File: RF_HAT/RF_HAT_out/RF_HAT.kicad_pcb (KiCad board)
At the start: 8 copper layers, 56 x 65 mm, 97 parts, among them J1 SMA, J2 SMA, J3 Raspberry_Pi_2_3, U1 CC1200RHBR, U2 CC1200RHBR, U3 RaspberryPi_Pico, U4 XT30PW-M, U5 LMR51420YFDDCR, Y1 40MHz, Y2 40MHz

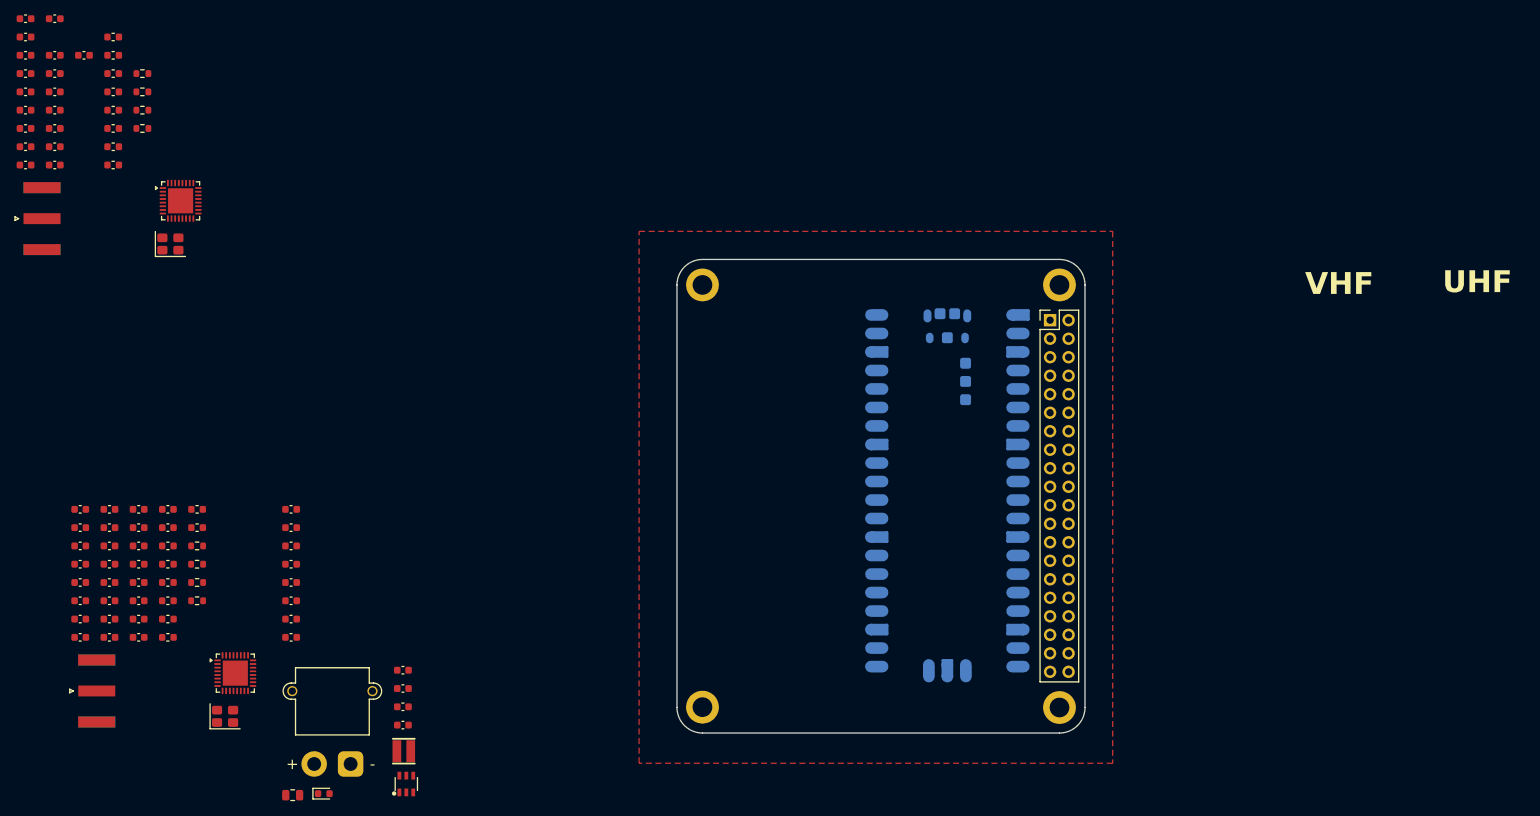
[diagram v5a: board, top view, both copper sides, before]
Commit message: did final routing and added Farnell and LCSC numbers to all components
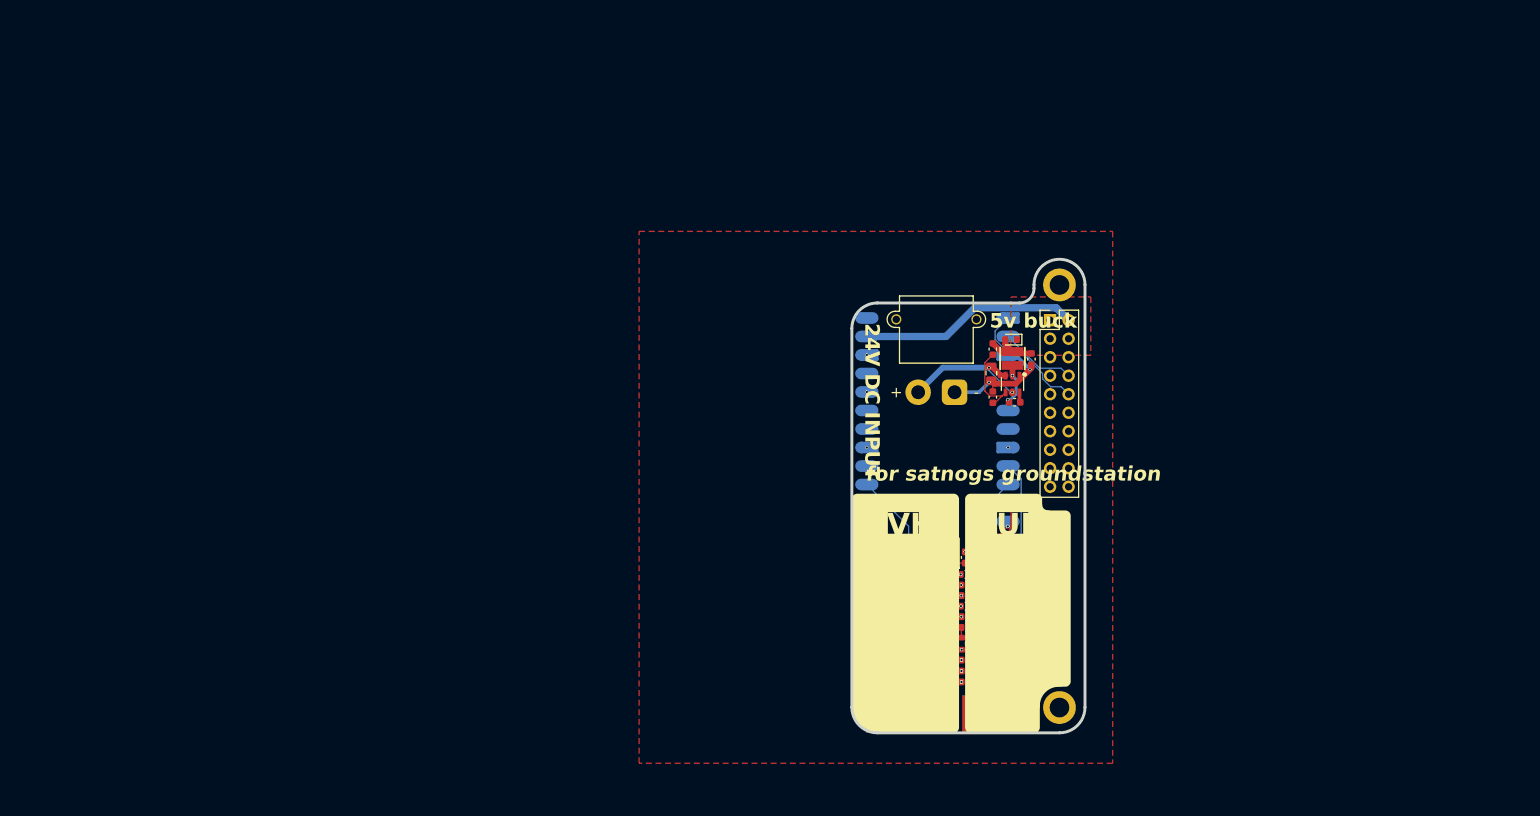
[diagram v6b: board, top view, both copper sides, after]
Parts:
- removed H2, H3: MountingHole_Pad, MountingHole:MountingHole_2.7mm_M2.5_ISO7380_Pad
- moved C1 160.1 mm to (205.9, 116.8), turned to -90 degrees
- moved C10 159.8 mm to (204.2, 124.2), turned to -90 degrees
- moved C3 158.7 mm to (207.4, 116.8), turned to 90 degrees
- moved C12 155.8 mm to (214.9, 105.0), turned to -90 degrees
- moved C2 155.0 mm to (204.2, 112.4), turned to -90 degrees
- moved C4 153.9 mm to (202.0, 118.8), turned to 180 degrees
- moved C8 153.7 mm to (210.4, 113.9), turned to -90 degrees
- moved C14 153.2 mm to (212.6, 108.7)
- moved C5 150.4 mm to (202.8, 113.6), turned to 90 degrees
- moved C13 150.3 mm to (213.1, 98.6)
- moved C15 150.1 mm to (212.6, 104.3)
- moved C21 150.0 mm to (208.9, 110.9), turned to -90 degrees
- moved C9 149.9 mm to (207.4, 113.9), turned to -90 degrees
- moved C6 149.7 mm to (202.0, 115.8), turned to 180 degrees
- moved C7 149.2 mm to (202.0, 117.3), turned to 180 degrees
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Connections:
- J3 pad 10: /Pi_Header/UART_RX -> /Pi_Header/UART_TX
- J3 pad 8: /Pi_Header/UART_TX -> /Pi_Header/UART_RX
- R1 pad 2: /CC1200_VHF_144MHz/UHF_CSN -> /CC1200_VHF_144MHz/VHF_CSN
- R2 pad 2: /CC1200_VHF_144MHz/UHF_RESET -> /CC1200_VHF_144MHz/VHF_RESET
- U2 pad 10: /CC1200_VHF_144MHz/UHF_GPIO0 -> /CC1200_VHF_144MHz/VHF_GPIO0
- U2 pad 11: /CC1200_VHF_144MHz/UHF_CSN -> /CC1200_VHF_144MHz/VHF_CSN
- U2 pad 2: /CC1200_VHF_144MHz/UHF_RESET -> /CC1200_VHF_144MHz/VHF_RESET
- U2 pad 3: /CC1200_VHF_144MHz/UHF_GPIO3 -> /CC1200_VHF_144MHz/VHF_GPIO3
- U2 pad 4: /CC1200_VHF_144MHz/UHF_GPIO2 -> /CC1200_VHF_144MHz/VHF_GPIO2
- U2 pad 7: /CC1200_VHF_144MHz/UHF_MOSI -> /CC1200_VHF_144MHz/VHF_MOSI
- U2 pad 8: /CC1200_VHF_144MHz/UHF_SCLK -> /CC1200_VHF_144MHz/VHF_SCLK
- U2 pad 9: /CC1200_VHF_144MHz/UHF_MISO -> /CC1200_VHF_144MHz/VHF_MISO
- U3 pad 21: /Pico_SPI_Host/VHF_MISO -> /CC1200_VHF_144MHz/VHF_MISO
- U3 pad 22: /Pico_SPI_Host/VHF_CSN -> /CC1200_VHF_144MHz/VHF_CSN
- U3 pad 24: /Pico_SPI_Host/VHF_SCLK -> /CC1200_VHF_144MHz/VHF_SCLK
- U3 pad 25: /Pico_SPI_Host/VHF_MOSI -> /CC1200_VHF_144MHz/VHF_MOSI
- U3 pad 26: /Pico_SPI_Host/VHF_RESET -> /CC1200_VHF_144MHz/VHF_RESET
- U3 pad 27: /Pico_SPI_Host/VHF_GPIO2 -> /CC1200_VHF_144MHz/VHF_GPIO2
- U3 pad 29: /Pico_SPI_Host/VHF_GPIO0 -> /CC1200_VHF_144MHz/VHF_GPIO0
- U3 pad 31: /Pico_SPI_Host/VHF_GPIO3 -> /CC1200_VHF_144MHz/VHF_GPIO3
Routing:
- net +3V3: track 0.00 -> 56.9 mm, vias 0 -> 31
- net GND: track 0.00 -> 34.7 mm, vias 0 -> 59
- net +5V: track 0.00 -> 30.0 mm
- net +24V: track 0.00 -> 18.9 mm, vias 0 -> 2
- net /Pi_Header/UART_TX: track 0.00 -> 17.3 mm
- net /CC1200_UHF_432MHz/UHF_GPIO3: track 0.00 -> 16.7 mm, vias 0 -> 1
- net /CC1200_VHF_144MHz/VHF_MISO: track 0.00 -> 15.6 mm, vias 0 -> 1
- net /CC1200_UHF_432MHz/UHF_GPIO0: track 0.00 -> 15.3 mm, vias 0 -> 1
- net /CC1200_VHF_144MHz/VHF_GPIO3: track 0.00 -> 14.1 mm, vias 0 -> 1
- net /CC1200_VHF_144MHz/VHF_CSN: track 0.00 -> 13.7 mm, vias 0 -> 1
- net Net-(U1-TRX_SW): track 0.00 -> 11.5 mm
- net Net-(U2-TRX_SW): track 0.00 -> 11.2 mm
- net /Pi_Header/UART_RX: track 0.00 -> 10.5 mm
- net Net-(U5-FB): track 0.00 -> 10.4 mm
- net /CC1200_UHF_432MHz/UHF_RESET: track 0.00 -> 10.3 mm, vias 0 -> 1
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- added copper zone on In2.Cu, net +3V3
- added copper zone on In3.Cu, net +3V3
- added copper zone on F.Cu, net GND
- added copper zone on In4.Cu, net GND
- removed copper zone on In4.Cu, net (none)
- removed copper zone on In4.Cu, net +3V3
- removed copper zone on In3.Cu, net GND
- removed copper zone on In5.Cu, net GND
- removed copper zone on In6.Cu, net GND
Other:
- board size 56 x 65 mm -> 32 x 65 mm
- copper layers 8 -> 6
- board text added: "-RF HAT-"
- board text added: "24V DC INPUT"
- board text added: "5v buck"
- board text added: "connect to any pi ----"
- board text added: "for satnogs groundstation"
- board text added: "pi zero, pi3, pi4, pi5..."

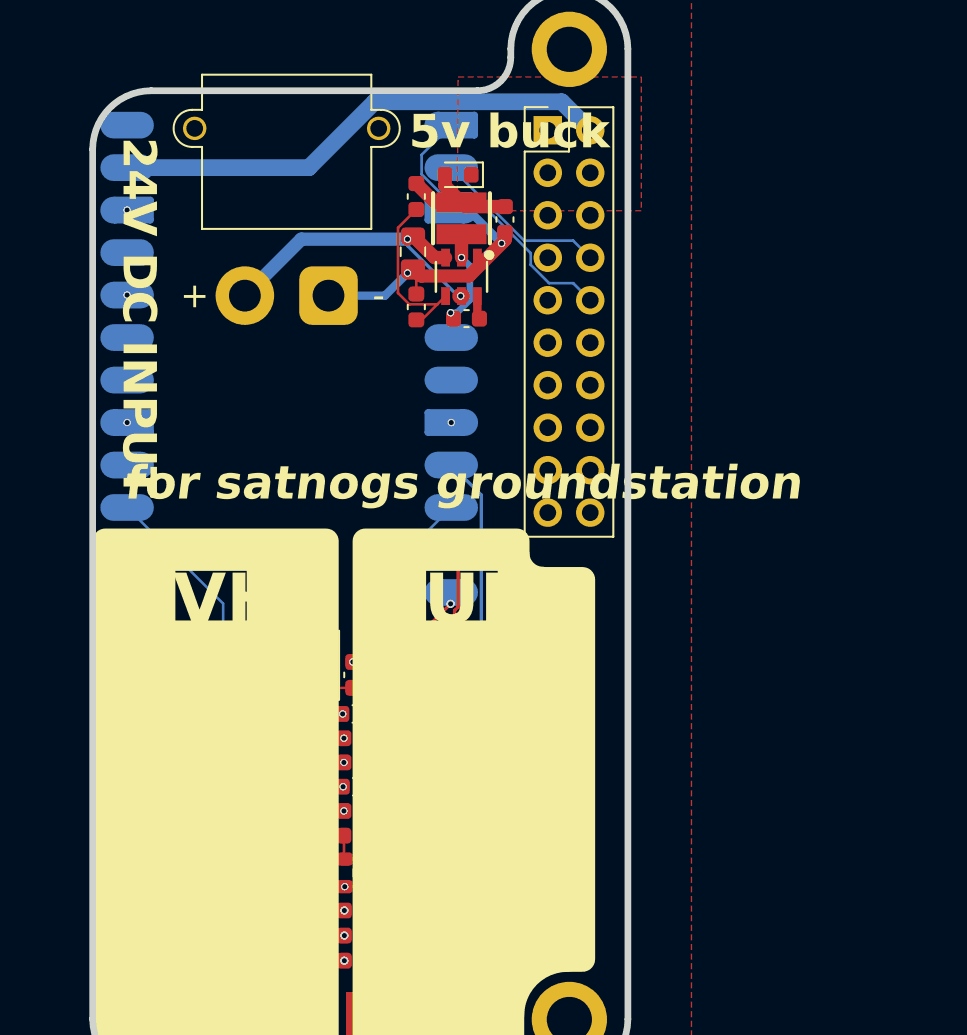
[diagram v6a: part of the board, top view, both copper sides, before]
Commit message: update RF_HAT to have WS2812 and buzzer. Start on webserver interface with demo visuals, integration in satnogs system, dual SPI and UART to USB on the Pi_HAT, update readme's
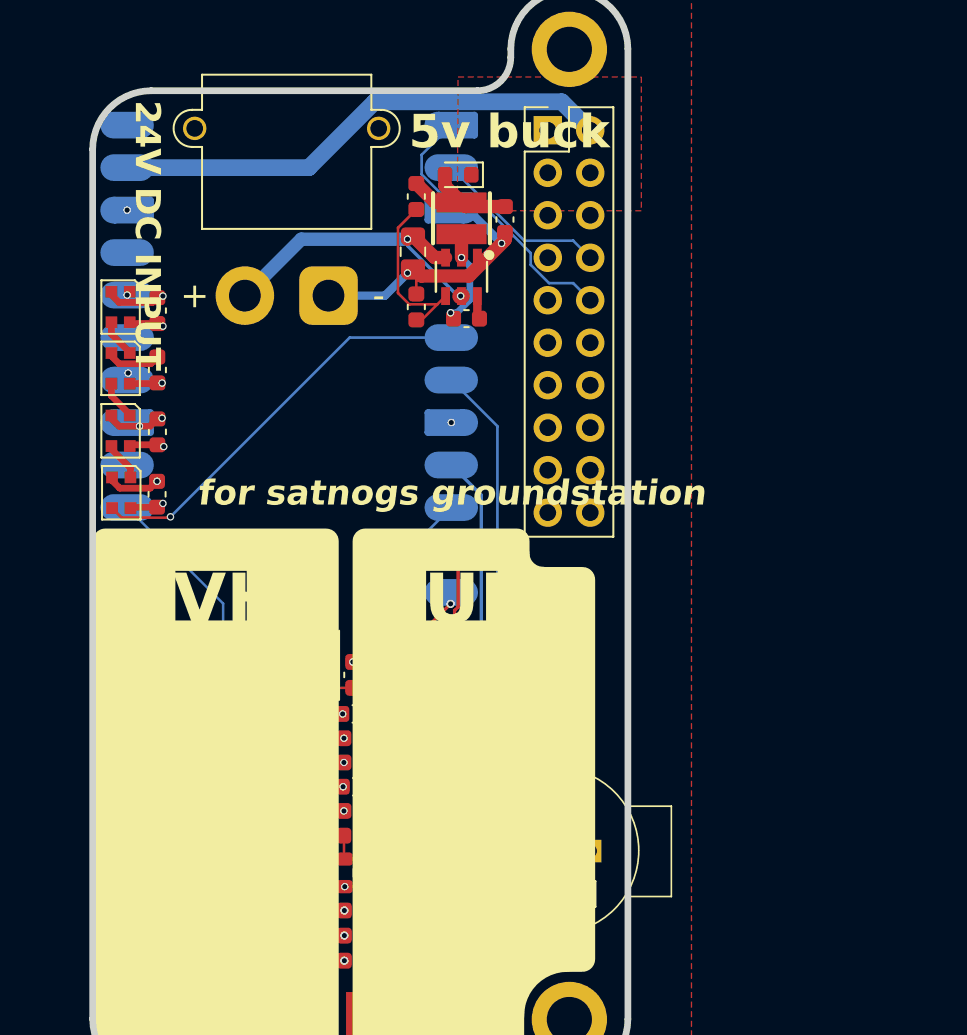
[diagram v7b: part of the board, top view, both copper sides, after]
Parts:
- added C48: 220nF, Capacitor_SMD:C_0603_1608Metric, F.Cu at (190.1, 91.0)
- added C49: 220nF, Capacitor_SMD:C_0603_1608Metric, F.Cu at (190.1, 87.2)
- added C50: 220nF, Capacitor_SMD:C_0603_1608Metric, F.Cu at (190.1, 83.5)
- added C51: 220nF, Capacitor_SMD:C_0603_1608Metric, F.Cu at (190.1, 80.0)
- added D2: 1N4148WS, Diode_SMD:D_SOD-323, F.Cu at (212.3, 114.8)
- added D3: WS2812B-2020, LED_SMD:LED_WS2812B-2020_PLCC4_2.0x2.0mm, F.Cu at (187.9, 90.9)
- added D4: WS2812B-2020, LED_SMD:LED_WS2812B-2020_PLCC4_2.0x2.0mm, F.Cu at (187.9, 87.2)
- added D5: WS2812B-2020, LED_SMD:LED_WS2812B-2020_PLCC4_2.0x2.0mm, F.Cu at (187.9, 83.4)
- added D6: WS2812B-2020, LED_SMD:LED_WS2812B-2020_PLCC4_2.0x2.0mm, F.Cu at (187.9, 79.8)
- added J4: Conn_01x01, Connector_PinHeader_2.00mm:PinHeader_1x01_P2.00mm_Vertical, B.Cu at (211.9, 112.3)
- added J5: Conn_01x01, Connector_PinHeader_2.00mm:PinHeader_1x01_P2.00mm_Vertical, B.Cu at (215.9, 112.3)
- added Q1: BSS138, Package_TO_SOT_SMD:SOT-23, F.Cu at (214.7, 114.8)
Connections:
- U3 pad 6: unconnected-(U3-GPIO4-Pad6) -> /WS2812B
- U3 pad 7: unconnected-(U3-GPIO5-Pad7) -> /Pico_SPI_Host/BUZZER
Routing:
- net /Pico_SPI_Host/BUZZER: track 0.00 -> 36.7 mm, vias 0 -> 1
- net /WS2812B: track 0.00 -> 25.0 mm, vias 0 -> 1
- net GND: track 34.7 -> 48.8 mm, vias 59 -> 63
- net +3V3: track 56.9 -> 66.8 mm, vias 31 -> 36
- net Net-(D2-A): track 0.00 -> 5.55 mm
- net Net-(D4-DOUT): track 0.00 -> 2.36 mm
- net Net-(D3-DOUT): track 0.00 -> 2.35 mm
- net Net-(D5-DOUT): track 0.00 -> 2.29 mm
- net unconnected-(U3-GPIO28_ADC2-Pad34): vias 0 -> 1
